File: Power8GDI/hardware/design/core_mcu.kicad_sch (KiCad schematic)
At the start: 31 parts, among them J101 SWD 3V3 target reference, U101 STM32F767IIT6, Y101 ASEM1-8.000MHZ-LC-T

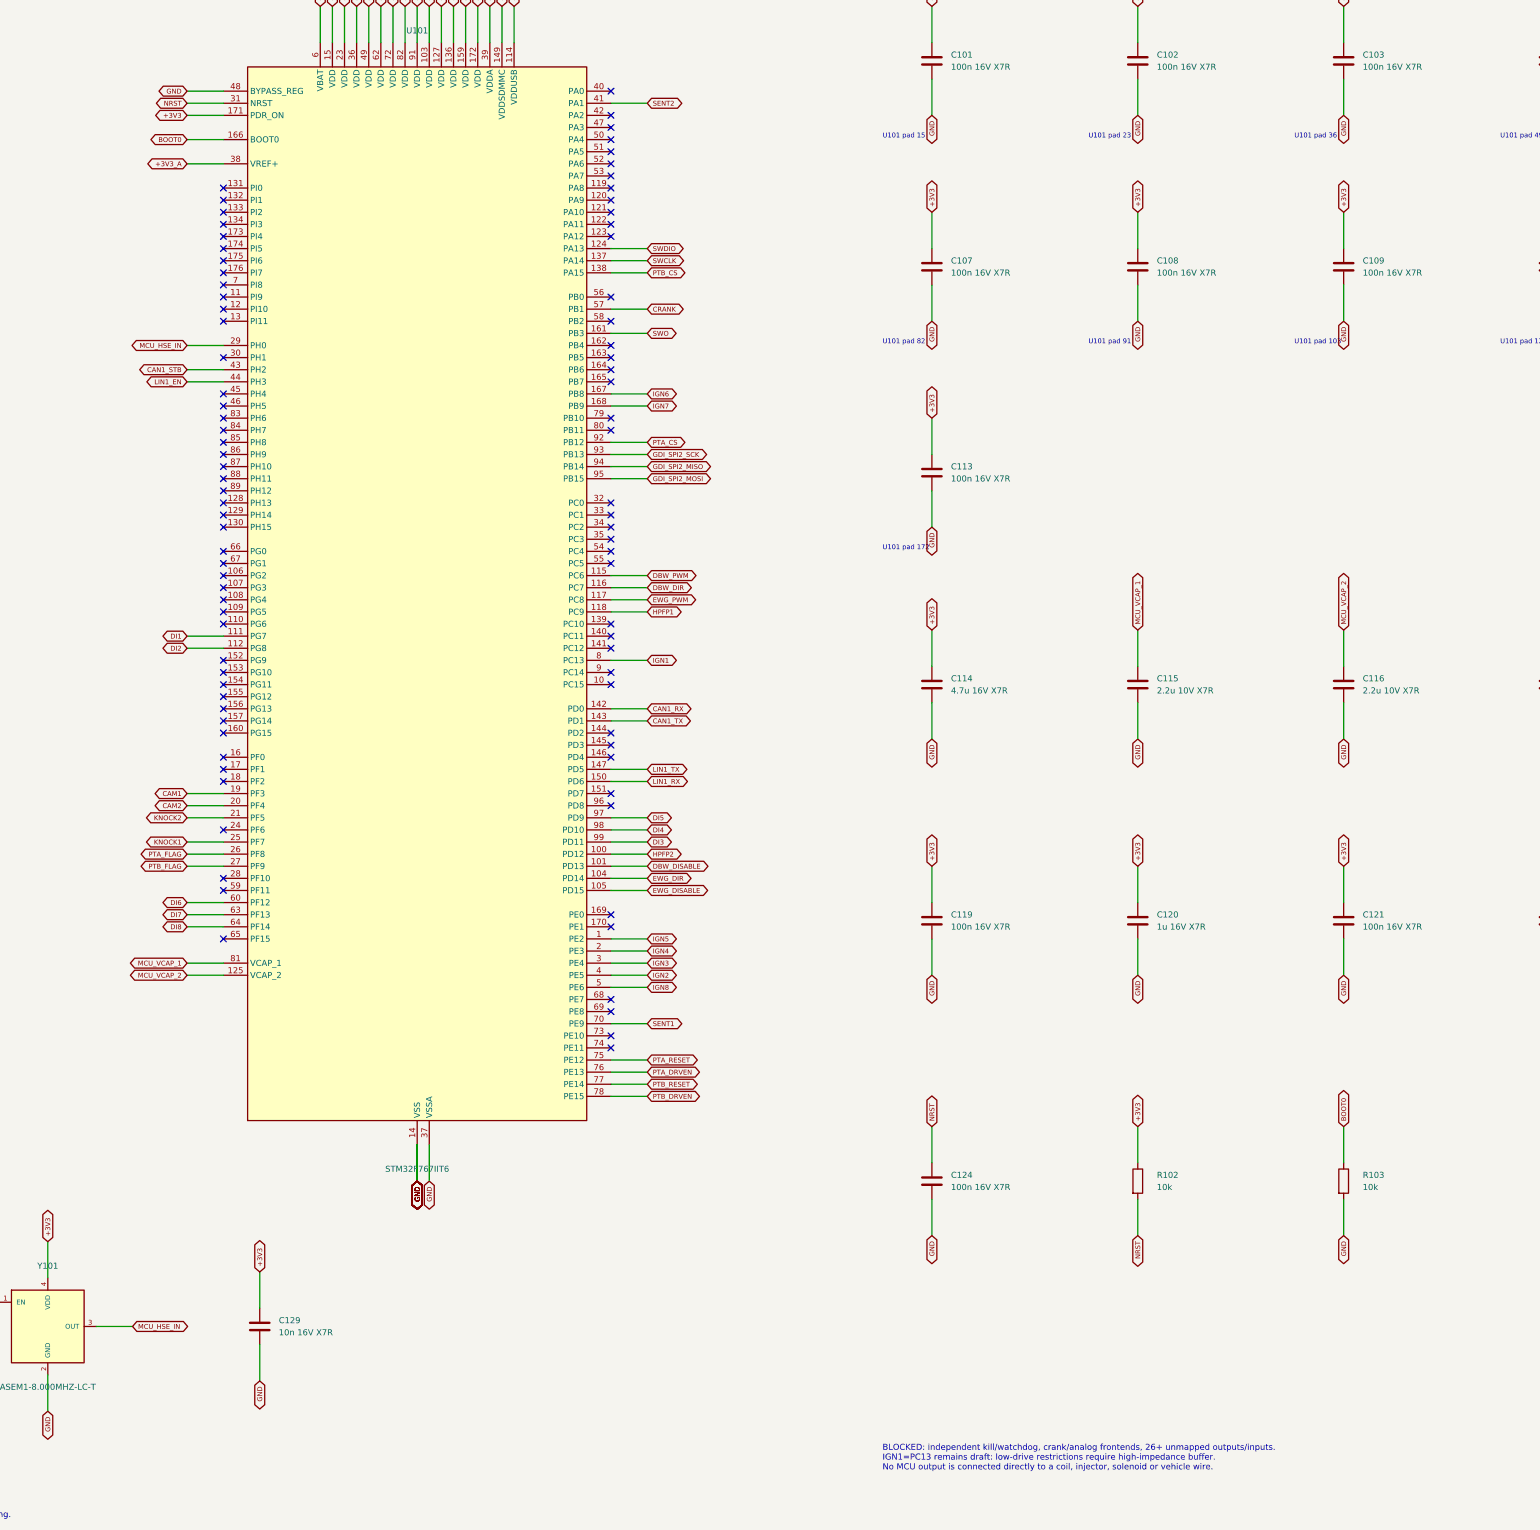
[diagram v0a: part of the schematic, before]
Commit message: Integrate connected ECU schematic and auditable review PCB
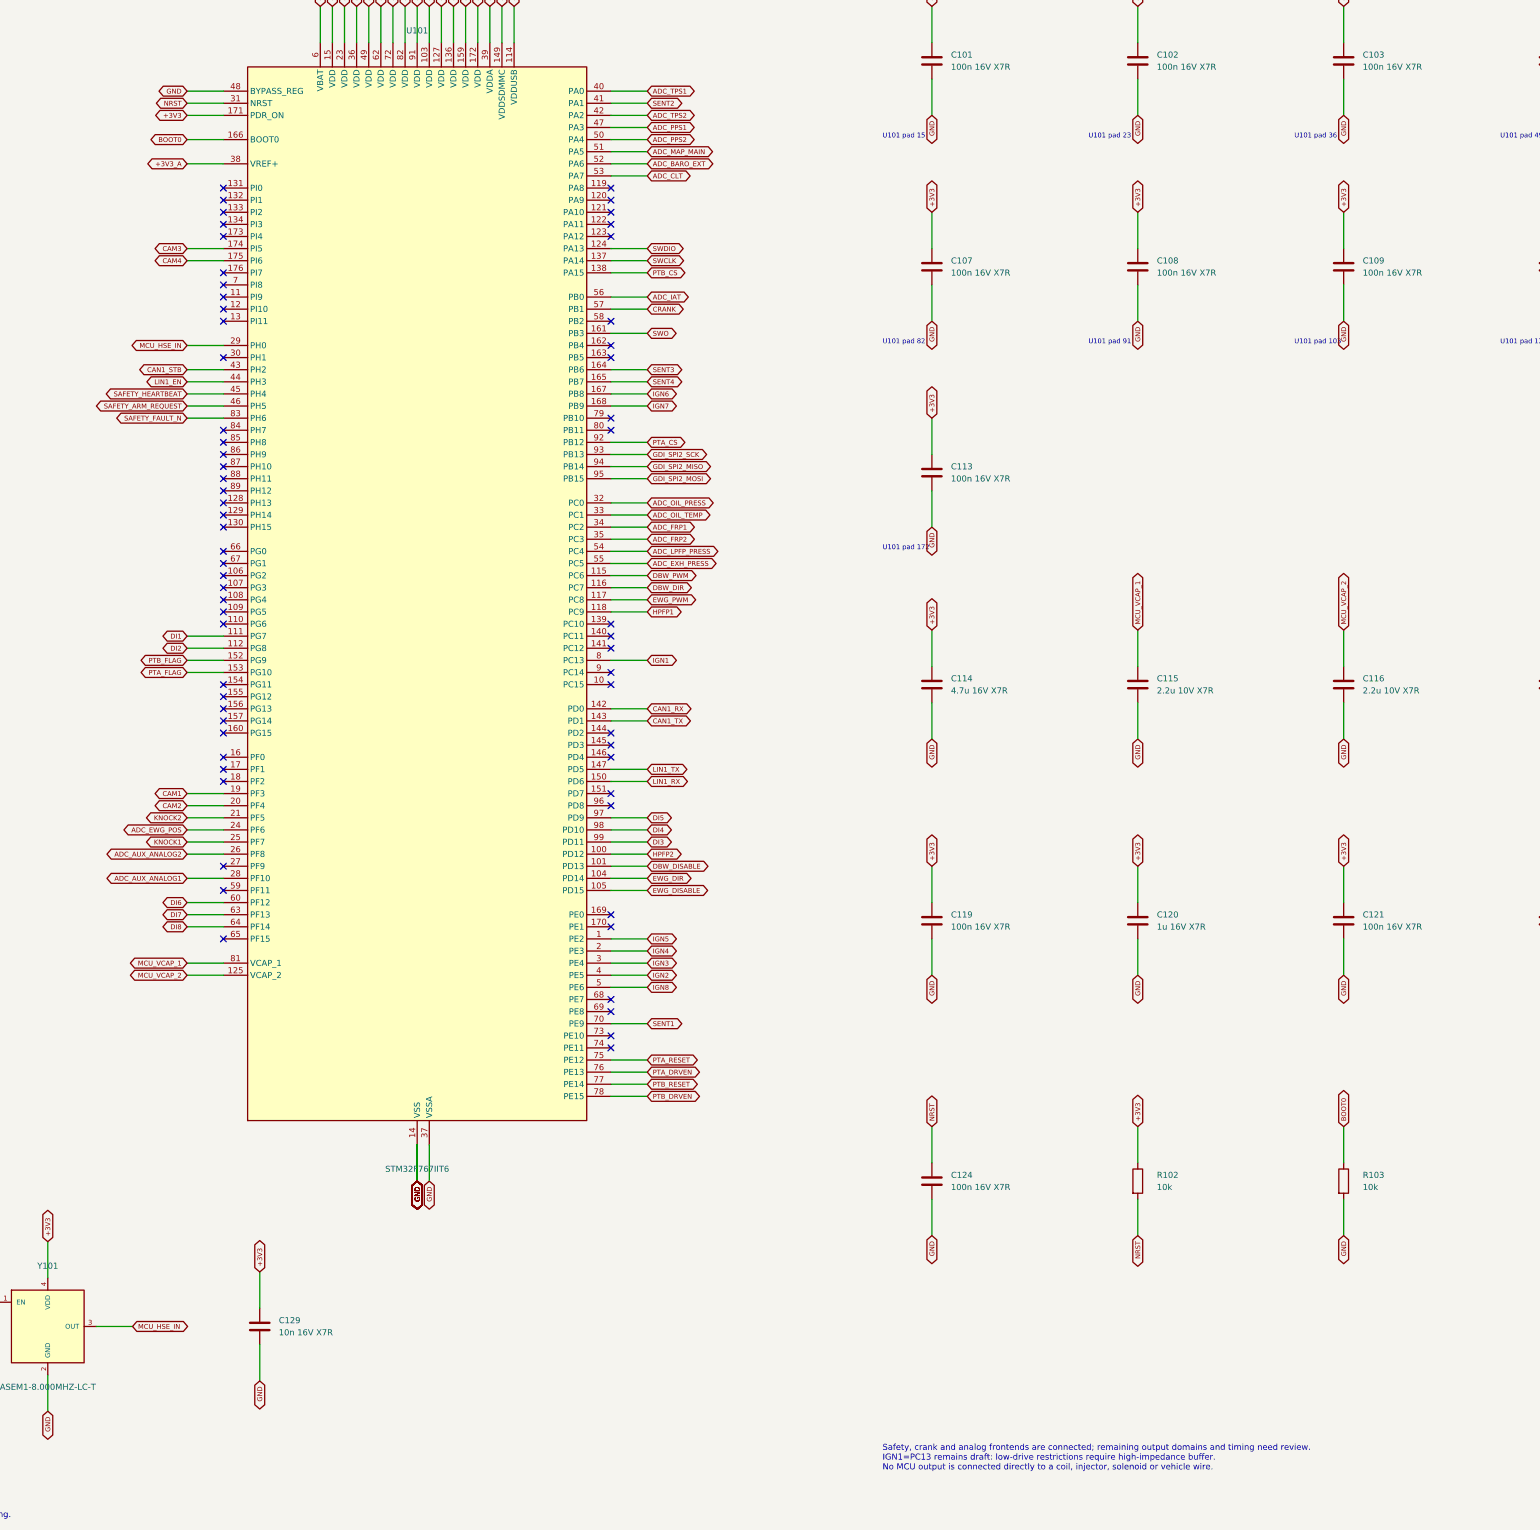
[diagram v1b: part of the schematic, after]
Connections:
- net PTA_FLAG: now also U101.153 (PG10); no longer U101.26 (PF8)
- net PTB_FLAG: now also U101.152 (PG9); no longer U101.27 (PF9)
- net SENT3: now reaches U101.164 (PB6)
- net SENT4: now reaches U101.165 (PB7)
- net CAM3: now reaches U101.174 (PI5)
- net CAM4: now reaches U101.175 (PI6)
- net ADC_EWG_POS: now reaches U101.24 (PF6)
- net ADC_AUX_ANALOG1: now reaches U101.28 (PF10)
- net ADC_OIL_PRESS: now reaches U101.32 (PC0)
- net ADC_OIL_TEMP: now reaches U101.33 (PC1)
- net ADC_FRP1: now reaches U101.34 (PC2)
- net ADC_FRP2: now reaches U101.35 (PC3)
- net ADC_TPS1: now reaches U101.40 (PA0)
- net ADC_TPS2: now reaches U101.42 (PA2)
- net SAFETY_HEARTBEAT: now reaches U101.45 (PH4)
- net SAFETY_ARM_REQUEST: now reaches U101.46 (PH5)
- net ADC_PPS1: now reaches U101.47 (PA3)
- net ADC_PPS2: now reaches U101.50 (PA4)
- net ADC_MAP_MAIN: now reaches U101.51 (PA5)
- net ADC_BARO_EXT: now reaches U101.52 (PA6)
- net ADC_CLT: now reaches U101.53 (PA7)
- net ADC_LPFP_PRESS: now reaches U101.54 (PC4)
- net ADC_EXH_PRESS: now reaches U101.55 (PC5)
- net ADC_IAT: now reaches U101.56 (PB0)
- net SAFETY_FAULT_N: now reaches U101.83 (PH6)
- new net ADC_AUX_ANALOG2: U101.26 (PF8)
- no-connect marks 90 -> 66
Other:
- note added: "Safety, crank and analog frontends are connected; remaining output domains and timing need review. IGN1=PC13 remains draft: low-drive restrictions require high-impedance buffer. No MCU output is connected directly to a coil, injector, solenoid or vehicle wire."
- note removed: "BLOCKED: independent kill/watchdog, crank/analog frontends, 26+ unmapped outputs/inputs. IGN1=PC13 remains draft: low-drive restrictions require high-impedance buffer. No MCU output is connected directly to a coil, injector, solenoid or vehicle wire."

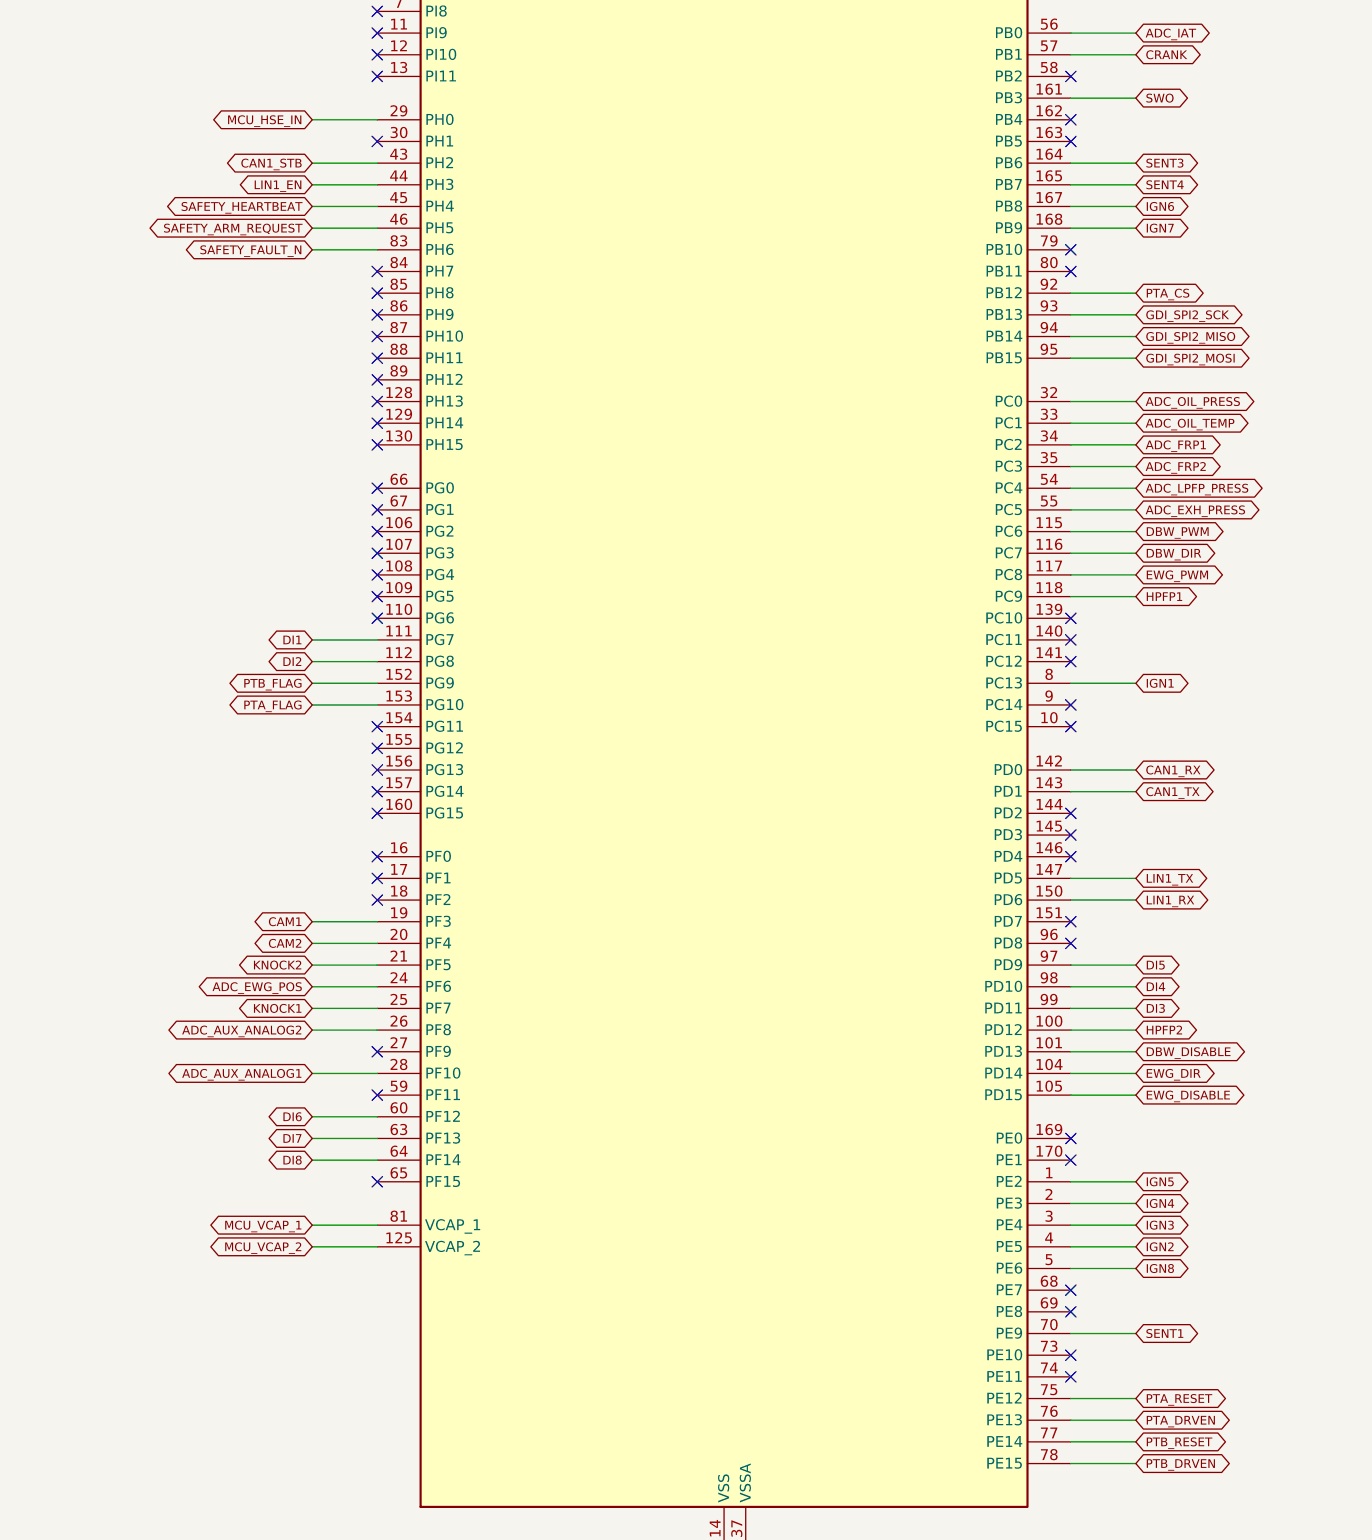
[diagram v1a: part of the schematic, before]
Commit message: Add 24 direct protected low-side output circuits with hardware inhibit
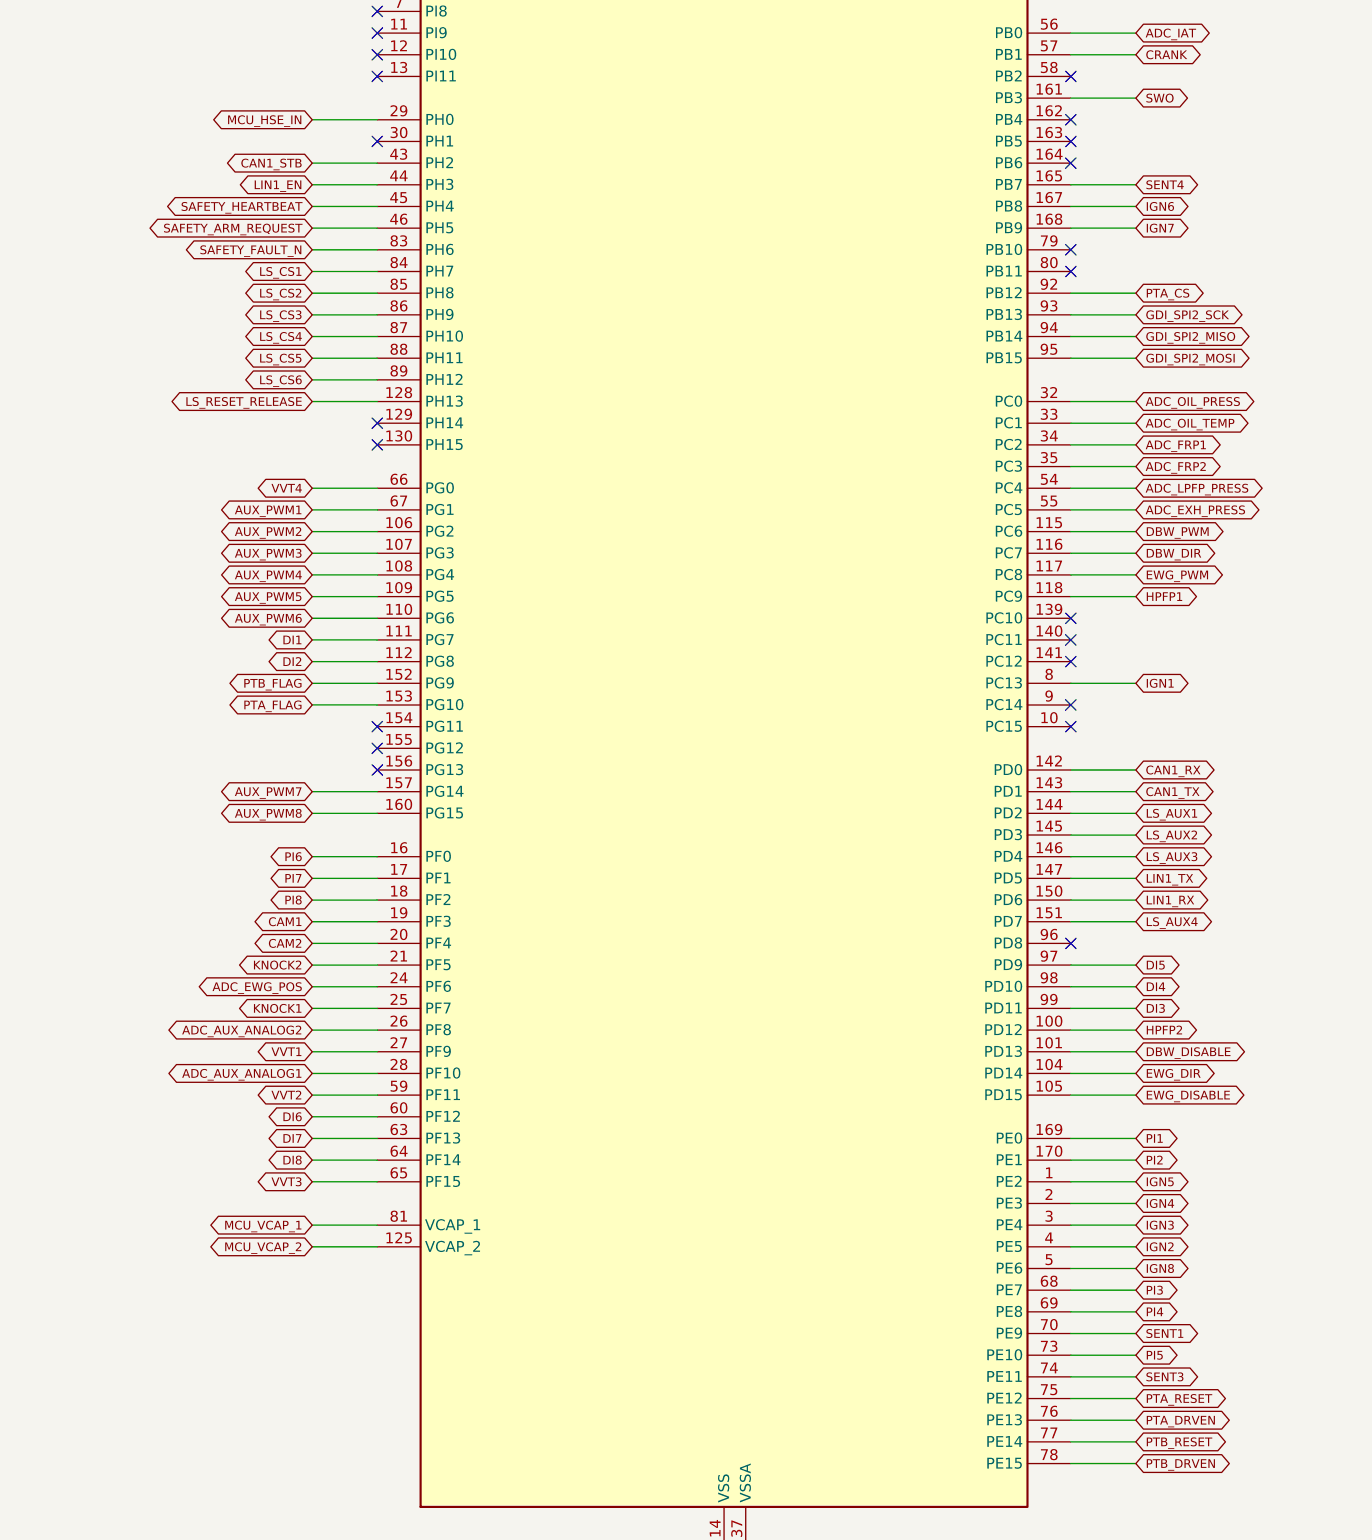
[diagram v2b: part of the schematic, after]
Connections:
- net SENT3: now also U101.74 (PE11); no longer U101.164 (PB6)
- net AUX_PWM2: now reaches U101.106 (PG2)
- net AUX_PWM3: now reaches U101.107 (PG3)
- net AUX_PWM4: now reaches U101.108 (PG4)
- net AUX_PWM5: now reaches U101.109 (PG5)
- net AUX_PWM6: now reaches U101.110 (PG6)
- net LS_RESET_RELEASE: now reaches U101.128 (PH13)
- net LS_AUX1: now reaches U101.144 (PD2)
- net LS_AUX2: now reaches U101.145 (PD3)
- net LS_AUX3: now reaches U101.146 (PD4)
- net LS_AUX4: now reaches U101.151 (PD7)
- net AUX_PWM7: now reaches U101.157 (PG14)
- net PI6: now reaches U101.16 (PF0)
- net AUX_PWM8: now reaches U101.160 (PG15)
- net PI1: now reaches U101.169 (PE0)
- net PI7: now reaches U101.17 (PF1)
- net PI2: now reaches U101.170 (PE1)
- net PI8: now reaches U101.18 (PF2)
- net VVT1: now reaches U101.27 (PF9)
- net VVT2: now reaches U101.59 (PF11)
- net VVT3: now reaches U101.65 (PF15)
- net VVT4: now reaches U101.66 (PG0)
- net AUX_PWM1: now reaches U101.67 (PG1)
- net PI3: now reaches U101.68 (PE7)
- net PI4: now reaches U101.69 (PE8)
- net PI5: now reaches U101.73 (PE10)
- net LS_CS1: now reaches U101.84 (PH7)
- net LS_CS2: now reaches U101.85 (PH8)
- net LS_CS3: now reaches U101.86 (PH9)
- net LS_CS4: now reaches U101.87 (PH10)
- net LS_CS5: now reaches U101.88 (PH11)
- net LS_CS6: now reaches U101.89 (PH12)
- no-connect marks 66 -> 35
